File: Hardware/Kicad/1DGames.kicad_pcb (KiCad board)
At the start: 16 copper layers, 530 x 140 mm, 96 parts, among them J1 5V_to_Rail_and_ESP_32_Proto_b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, J10 Edge Pads Right (GND), J13 Edge_Pads_Right_Top, J14 5V LED Strips Long Side Rail, J15 Edge_Pads_Right_Bottom, J16 GND Long Side Rail, J17 MCP23017_Control, J18 Player1_TM1637, J19 CP TM1637, J2 MAX98357_AMPLIFIER_MODULE_OUT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, J20 Player2_TM1637, J22 MCP23017_Gpios, J23 Edge_Pads_Left_Top, J24 Edge_Pads_Left_Bottom, J26 5V/GND from Power Board, J31 MAX98357_AMPLIFIER_MODULE, J32 LCD1602, J34 INMP441_LEFT, J35 INMP441_RIGHT, J36 Led Strip 1 Begin, J37 Led Strip 2 Begin, J38 Led Strip 3 Begin, J39 Led Strip 4 Begin, J40 Led Strip 5 Begin, J42 Led Strip 1 End, J43 Led Strip 2 End, J44 Led Strip 3 End, J45 Led Strip 4 End, J46 Led Strip 5 End, J5 Micro SD Card Reader, J6 5V_15A_Power, J7 DE9_Socket, J8 DE9_Socket, J9 Edge Pads Left (5V), P1 IEC_60320_C13_Plug, Q1 2N2222, SW1 System_Button, U1 AMS1117-3.3, U3 BOB-12009, U4 DEVKIT_V1_ESP32-WROOM-32, U5 74AHCT125

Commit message: Replaced 1602 to 2004 in Kicad and Tinkercad
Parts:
- R26: value 4.7K -> 10K
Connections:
- net /ESP32 & SPI/I2S_BCLK renamed /Audio (page 4) (pagina 4)/I2S_BCLK
- net /ESP32 & SPI/I2S_INMP441_DIN renamed /Audio (page 4) (pagina 4)/I2S_INMP441_DIN
- net /ESP32 & SPI/I2S_MAX98357 renamed /Audio (page 4) (pagina 4)/I2S_MAX98357
- net /ESP32 & SPI/I2S_WS_LRCLK renamed /Audio (page 4) (pagina 4)/I2S_WS_LRCLK
- net /ESP32 & SPI/PASSIVE_BUZZER_SIGNAL renamed /Audio (page 4) (pagina 4)/PASSIVE_BUZZER_SIGNAL
- net /Edge Pads/5V_BUZZER_EXT renamed /Audio (page 4) (pagina 4)/5V_BUZZER_EXT
- net /Edge Pads/I2S_BCLK_OUT renamed /Audio (page 4) (pagina 4)/I2S_BCLK_OUT
- net /Edge Pads/I2S_WS_LRCLK_OUT renamed /Audio (page 4) (pagina 4)/I2S_WS_LRCLK_OUT
- C14 pad 1: /ESP32 & SPI/3V3 -> /Audio (page 4) (pagina 4)/3V3
- C19 pad 1: /I2C/SYSTEM_BUTTON -> /Audio (page 4) (pagina 4)/3V3
- C4 pad 2: /ESP32 & SPI/3V3 -> /Audio (page 4) (pagina 4)/3V3
- C5 pad 2: /ESP32 & SPI/3V3 -> /Audio (page 4) (pagina 4)/3V3
- J17 pad 1: /ESP32 & SPI/3V3 -> /Audio (page 4) (pagina 4)/3V3
- J17 pad 7: /ESP32 & SPI/3V3 -> /Audio (page 4) (pagina 4)/3V3
- J22 pad 2: /ESP32 & SPI/3V3 -> /Audio (page 4) (pagina 4)/3V3
- J23 pad 1: /ESP32 & SPI/3V3 -> /Audio (page 4) (pagina 4)/3V3
- J23 pad 10: /ESP32 & SPI/3V3 -> /Audio (page 4) (pagina 4)/3V3
- J23 pad 11: /ESP32 & SPI/3V3 -> /Audio (page 4) (pagina 4)/3V3
- J23 pad 12: /ESP32 & SPI/3V3 -> /Audio (page 4) (pagina 4)/3V3
- J23 pad 13: /ESP32 & SPI/3V3 -> /Audio (page 4) (pagina 4)/3V3
- J23 pad 2: /ESP32 & SPI/3V3 -> /Audio (page 4) (pagina 4)/3V3
- J23 pad 3: /ESP32 & SPI/3V3 -> /Audio (page 4) (pagina 4)/3V3
- J23 pad 4: /ESP32 & SPI/3V3 -> /Audio (page 4) (pagina 4)/3V3
- J23 pad 5: /ESP32 & SPI/3V3 -> /Audio (page 4) (pagina 4)/3V3
- J23 pad 6: /ESP32 & SPI/3V3 -> /Audio (page 4) (pagina 4)/3V3
- J23 pad 7: /ESP32 & SPI/3V3 -> /Audio (page 4) (pagina 4)/3V3
- J23 pad 8: /ESP32 & SPI/3V3 -> /Audio (page 4) (pagina 4)/3V3
- J23 pad 9: /ESP32 & SPI/3V3 -> /Audio (page 4) (pagina 4)/3V3
- J31 pad 5: /ESP32 & SPI/3V3 -> /Audio (page 4) (pagina 4)/3V3
- J34 pad 2: /ESP32 & SPI/3V3 -> /Audio (page 4) (pagina 4)/3V3
- R1 pad 1: /ESP32 & SPI/3V3 -> /Audio (page 4) (pagina 4)/3V3
- R17 pad 1: /ESP32 & SPI/3V3 -> /Audio (page 4) (pagina 4)/3V3
- R18 pad 1: /ESP32 & SPI/3V3 -> /Audio (page 4) (pagina 4)/3V3
- R19 pad 1: /ESP32 & SPI/3V3 -> /Audio (page 4) (pagina 4)/3V3
- R2 pad 2: /ESP32 & SPI/3V3 -> /Audio (page 4) (pagina 4)/3V3
- R20 pad 1: /ESP32 & SPI/3V3 -> /Audio (page 4) (pagina 4)/3V3
- R21 pad 1: /ESP32 & SPI/3V3 -> /Audio (page 4) (pagina 4)/3V3
- R22 pad 1: /ESP32 & SPI/3V3 -> /Audio (page 4) (pagina 4)/3V3
- R23 pad 1: /ESP32 & SPI/3V3 -> /Audio (page 4) (pagina 4)/3V3
- R24 pad 1: /ESP32 & SPI/3V3 -> /Audio (page 4) (pagina 4)/3V3
- R25 pad 1: /ESP32 & SPI/3V3 -> /Audio (page 4) (pagina 4)/3V3
- R26 pad 1: /ESP32 & SPI/3V3 -> /Audio (page 4) (pagina 4)/3V3
- R28 pad 1: /ESP32 & SPI/3V3 -> /Audio (page 4) (pagina 4)/3V3
- U1 pad 2: /ESP32 & SPI/3V3 -> /Audio (page 4) (pagina 4)/3V3
- U3 pad LV: /ESP32 & SPI/3V3 -> /Audio (page 4) (pagina 4)/3V3
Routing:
- net /ESP32 & SPI/3V3: track 1167.3 -> 0.00 mm, vias 9 -> 0
- net /Audio (page 4) (pagina 4)/3V3: track 0.00 -> 1167.3 mm, vias 0 -> 9

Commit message: New architecture, L1 composition finished, probably, on ESP32
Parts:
- added R29: 10K, Resistor_THT:R_Axial_DIN0204_L3.6mm_D1.6mm_P5.08mm_Horizontal, F.Cu at (326.7, 358.6)
- J32: value LCD1602 -> LCD2004
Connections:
- J22 pad 3: unconnected-(J22-Pin_3-Pad3) -> /ESP32 & SPI/MCP23017_INT_AB
- U4 pad 13: unconnected-(U4-IO12-Pad13) -> /ESP32 & SPI/MCP23017_INT_AB
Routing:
- net /Audio (page 4) (pagina 4)/3V3: track 1167.3 -> 1586.5 mm, vias 9 -> 11
- net /ESP32 & SPI/MCP23017_INT_AB: track 0.00 -> 49.7 mm
- net /I2C/SYSTEM_BUTTON: track 218.5 -> 208.6 mm

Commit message: Broken code, halfway joystick gdi
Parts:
- added C20: 100 nF, Capacitor_THT:CP_Radial_D5.0mm_P2.50mm, F.Cu at (442.6, 415.8)
- added C21: 100 nF, Capacitor_THT:CP_Radial_D5.0mm_P2.50mm, F.Cu at (442.6, 422.3)
- added C22: 100 nF, Capacitor_THT:CP_Radial_D5.0mm_P2.50mm, F.Cu at (442.6, 428.9)
- added C23: 100 nF, Capacitor_THT:CP_Radial_D5.0mm_P2.50mm, F.Cu at (442.6, 435.4)
- added U10: HC-SR04_Ultrasonic_Sensor, PCM_SL_Breakout_Boards:HC-SR04_Ultrasonic_Sensor, F.Cu at (686.2, 332.9)
- added U11: HC-SR04_Ultrasonic_Sensor, PCM_SL_Breakout_Boards:HC-SR04_Ultrasonic_Sensor, F.Cu at (163.2, 273.0)
- added U7: BOB-12009, BOB-12009:CONV_BOB-12009, F.Cu at (284.7, 355.8)
- added U8: HC-SR04_Ultrasonic_Sensor, PCM_SL_Breakout_Boards:HC-SR04_Ultrasonic_Sensor, F.Cu at (159.2, 381.5)
- added U9: HC-SR04_Ultrasonic_Sensor, PCM_SL_Breakout_Boards:HC-SR04_Ultrasonic_Sensor, F.Cu at (685.2, 284.2)
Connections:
- J23 pad 16: unconnected-(J23-Pin_16-Pad16) -> /Edge Pads/HC_SR04_ECHO_1
- J23 pad 17: unconnected-(J23-Pin_17-Pad17) -> /Edge Pads/HC_SR04_TRIG_1
- J23 pad 18: unconnected-(J23-Pin_18-Pad18) -> /Edge Pads/HC_SR04_ECHO_2
- J23 pad 19: unconnected-(J23-Pin_19-Pad19) -> /Edge Pads/HC_SR04_TRIG_2
- J23 pad 20: unconnected-(J23-Pin_20-Pad20) -> /Edge Pads/HC_SR04_ECHO_3
- J23 pad 21: unconnected-(J23-Pin_21-Pad21) -> /Edge Pads/HC_SR04_TRIG_3
- J23 pad 22: unconnected-(J23-Pin_22-Pad22) -> /Edge Pads/HC_SR04_ECHO_4
- J23 pad 23: unconnected-(J23-Pin_23-Pad23) -> /Edge Pads/HC_SR04_TRIG_4
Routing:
- net /Audio (page 4) (pagina 4)/3V3: track 1586.5 -> 1625.2 mm
- net GND: track 7278.8 -> 7306.2 mm
- net /ESP32 & SPI/5V_BOARD: track 1469.0 -> 1487.2 mm
- net /Audio (page 4) (pagina 4)/PASSIVE_BUZZER_SIGNAL: track 85.9 -> 91.3 mm

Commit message: Added Kicad proto board
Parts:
- removed BZ1: Buzzer_5V, Buzzer_Beeper:MagneticBuzzer_ProSignal_ABT-410-RC
- removed C1, C10, C13, C7, C8: 0.1uF, Capacitor_THT:C_Disc_D3.0mm_W1.6mm_P2.50mm
- removed C12: 10-47uF, Capacitor_THT:CP_Radial_D5.0mm_P2.50mm
- removed C14: 1-10uF, Capacitor_THT:CP_Radial_D5.0mm_P2.50mm
- removed C15: 1000 uF, Capacitor_THT:CP_Radial_D10.0mm_P2.50mm
- removed C18: 100uF, Capacitor_THT:CP_Radial_D5.0mm_P2.50mm
- removed C19: 100nF, Capacitor_THT:CP_Radial_D5.0mm_P2.50mm
- removed C20, C21, C22, C23: 100 nF, Capacitor_THT:CP_Radial_D5.0mm_P2.50mm
- removed D2: Player 1 LED, LED_THT:LED_D5.0mm
- removed D3: Player 2 LED, LED_THT:LED_D5.0mm
- removed D4, D5, D6: LED, LED_THT:LED_D5.0mm
- removed J13: Edge_Pads_Right_Top, Connector_PinHeader_2.54mm:PinHeader_1x27_P2.54mm_Vertical_SMD_Pin1Left
- removed J14: 5V LED Strips Long Side Rail, Connector_PinHeader_2.54mm:PinHeader_1x10_P2.54mm_Vertical_SMD_Pin1Left
- removed J15: Edge_Pads_Right_Bottom, Connector_PinHeader_2.54mm:PinHeader_1x27_P2.54mm_Vertical_SMD_Pin1Left
- removed J16: GND Long Side Rail, Connector_PinHeader_2.54mm:PinHeader_1x16_P2.54mm_Vertical_SMD_Pin1Left
- removed J18: Player1_TM1637, PCM_SparkFun-Connector:ScrewTerminal_1x04_P3.5mm_Locking
- removed J19: CP TM1637, PCM_SparkFun-Connector:ScrewTerminal_1x04_P3.5mm_Locking
- removed J2: MAX98357_AMPLIFIER_MODULE_OUTPUT, PCM_SparkFun-Connector:ScrewTerminal_1x02_P5.0mm
- removed J20: Player2_TM1637, PCM_SparkFun-Connector:ScrewTerminal_1x04_P3.5mm_Locking
- removed J23: Edge_Pads_Left_Top, Connector_PinHeader_2.54mm:PinHeader_1x27_P2.54mm_Vertical_SMD_Pin1Left
- removed J24: Edge_Pads_Left_Bottom, Connector_PinHeader_2.54mm:PinHeader_1x27_P2.54mm_Vertical_SMD_Pin1Left
- removed J32: LCD2004, PCM_SparkFun-Connector:ScrewTerminal_1x04_P3.5mm_Horizontal
- removed J34: INMP441_LEFT, TerminalBlock_TE-Connectivity:TerminalBlock_TE_282834-3_1x03_P2.54mm_Horizontal
- removed J35: INMP441_RIGHT, TerminalBlock_TE-Connectivity:TerminalBlock_TE_282834-3_1x03_P2.54mm_Horizontal
- removed J36: Led Strip 1 Begin, PCM_SparkFun-Connector:ScrewTerminal_1x03_P5.0mm
- removed J37: Led Strip 2 Begin, PCM_SparkFun-Connector:ScrewTerminal_1x03_P5.0mm
- removed J38: Led Strip 3 Begin, PCM_SparkFun-Connector:ScrewTerminal_1x03_P5.0mm
- removed J39: Led Strip 4 Begin, PCM_SparkFun-Connector:ScrewTerminal_1x03_P5.0mm
- removed J40: Led Strip 5 Begin, PCM_SparkFun-Connector:ScrewTerminal_1x03_P5.0mm
- removed J42: Led Strip 1 End, PCM_SparkFun-Connector:ScrewTerminal_1x03_P5.0mm
- removed J43: Led Strip 2 End, PCM_SparkFun-Connector:ScrewTerminal_1x03_P5.0mm
- removed J44: Led Strip 3 End, PCM_SparkFun-Connector:ScrewTerminal_1x03_P5.0mm
- removed J45: Led Strip 4 End, PCM_SparkFun-Connector:ScrewTerminal_1x03_P5.0mm
- removed J46: Led Strip 5 End, PCM_SparkFun-Connector:ScrewTerminal_1x03_P5.0mm
- removed J7, J8: DE9_Socket, PCM_SparkFun-Connector:DE9_Header_Horizontal_PTH
- removed LS1: Speaker, Buzzer_Beeper:Speaker_CUI_CMR-1206S-67
- removed P1: IEC_60320_C13_Plug, Connector_PinHeader_2.54mm:PinHeader_1x03_P2.54mm_Vertical
- removed R10, R11, R13, R14, R15, R16: 100-200R, Resistor_THT:R_Axial_DIN0204_L3.6mm_D1.6mm_P5.08mm_Horizontal
- removed R12, R9: 100R, Resistor_THT:R_Axial_DIN0204_L3.6mm_D1.6mm_P5.08mm_Horizontal
- removed R29: 10K, Resistor_THT:R_Axial_DIN0204_L3.6mm_D1.6mm_P5.08mm_Horizontal
- removed SW1: System_Button, Button_Switch_THT:SW_CW_GPTS203211B
- removed U10, U11, U8, U9: HC-SR04_Ultrasonic_Sensor, PCM_SL_Breakout_Boards:HC-SR04_Ultrasonic_Sensor
- removed U4: DEVKIT_V1_ESP32-WROOM-32, PCM_Espressif:ESP32-DevKitC
- added H1: MountingHole_M3, MountingHole:MountingHole_3.2mm_M3, F.Cu at (398.0, 272.8)
- added H2: MountingHole_M3, MountingHole:MountingHole_3.2mm_M3, F.Cu at (378.4, 363.9)
- added H3: MountingHole_M3, MountingHole:MountingHole_3.2mm_M3, F.Cu at (305.4, 335.6)
- added H4: MountingHole_M3, MountingHole:MountingHole_3.2mm_M3, F.Cu at (307.6, 283.6)
- added J11: Conn_01x03, Connector_JST:JST_XH_B3B-XH-A_1x03_P2.50mm_Vertical, F.Cu at (383.0, 274.6)
- added J25: Conn_01x06, Connector_JST:JST_XH_B6B-XH-A_1x06_P2.50mm_Vertical, F.Cu at (397.5, 363.8)
- added J27: Conn_01x06, Connector_JST:JST_XH_B6B-XH-A_1x06_P2.50mm_Vertical, F.Cu at (363.5, 274.6)
- added J3: Conn_01x05, Connector_JST:JST_XH_B5B-XH-A_1x05_P2.50mm_Vertical, F.Cu at (346.5, 274.6)
- added J4: Conn_01x05, Connector_JST:JST_XH_B5B-XH-A_1x05_P2.50mm_Vertical, F.Cu at (329.5, 274.6)
- added R30: 150, PCM_Resistor_SMD_AKL:R_0805_2012Metric_Pad1.20x1.40mm_HandSolder, F.Cu at (381.2, 357.8)
- added R31: 150, PCM_Resistor_SMD_AKL:R_0805_2012Metric_Pad1.20x1.40mm_HandSolder, F.Cu at (383.8, 357.8)
- added R32: 150R, PCM_Resistor_SMD_AKL:R_0805_2012Metric_Pad1.20x1.40mm_HandSolder, F.Cu at (388.8, 348.3)
- added R33: 150R, PCM_Resistor_SMD_AKL:R_0805_2012Metric_Pad1.20x1.40mm_HandSolder, F.Cu at (388.8, 350.8)
- added R34: 150R, PCM_Resistor_SMD_AKL:R_0805_2012Metric_Pad1.20x1.40mm_HandSolder, F.Cu at (388.8, 345.8)
- added R35: 100, PCM_Resistor_SMD_AKL:R_0805_2012Metric_Pad1.20x1.40mm_HandSolder, F.Cu at (391.2, 357.8)
- added R36: 100, PCM_Resistor_SMD_AKL:R_0805_2012Metric_Pad1.20x1.40mm_HandSolder, F.Cu at (388.8, 357.8)
- added R37: 150R, PCM_Resistor_SMD_AKL:R_0805_2012Metric_Pad1.20x1.40mm_HandSolder, F.Cu at (388.8, 343.3)
- added REF**: KiCad-Logo2_6mm_SilkScreen, Symbol:KiCad-Logo2_6mm_SilkScreen, F.Cu at (331.0, 311.9)
- added U12: ESP32-S3-DEVKIT-C1, PCM_Espressif:ESP32-S3-DevKitC, F.Cu at (309.4, 366.4)
- C11, C16, C17, C2, C4: footprint Capacitor_THT:C_Disc_D3.0mm_W1.6mm_P2.50mm -> Capacitor_SMD:C_0805_2012Metric_Pad1.18x1.45mm_HandSolder
- C3, C5: value 10-22uF -> 22uF
- D1: footprint PCM_Diode_THT_AKL:D_DO-41_SOD81_P7.62mm_Horizontal -> Diode_SMD:D_SOD-123
- J1: value 5V_to_Rail_and_ESP_32_Proto_board -> Conn_01x06; footprint PCM_SparkFun-Connector:ScrewTerminal_1x03_P5.0mm -> Connector_JST:JST_XH_B6B-XH-A_1x06_P2.50mm_Vertical
- J10: value Edge Pads Right (GND) -> LED Strips Output; footprint Connector_PinSocket_2.54mm:PinSocket_1x04_P2.54mm_Vertical_SMD_Pin1Left -> TerminalBlock_Phoenix:TerminalBlock_Phoenix_MKDS-1,5-4_1x04_P5.00mm_Horizontal
- J26: value 5V/GND from Power Board -> 5V/GND Rail; footprint PCM_SparkFun-Connector:ScrewTerminal_1x02_P5.0mm -> TerminalBlock_Phoenix:TerminalBlock_Phoenix_MKDS-1,5-2_1x02_P5.00mm_Horizontal
- J6: value 5V_15A_Power -> Conn_01x06; footprint Connector_PinSocket_2.54mm:PinSocket_1x07_P2.54mm_Vertical -> Connector_JST:JST_XH_B6B-XH-A_1x06_P2.50mm_Vertical
- J9: value Edge Pads Left (5V) -> Power In; footprint Connector_PinSocket_2.54mm:PinSocket_1x04_P2.54mm_Vertical_SMD_Pin1Left -> TerminalBlock_Phoenix:TerminalBlock_Phoenix_MKDS-1,5-4_1x04_P5.00mm_Horizontal
- R1, R17, R18, R19, R2, R20, R21, R22, R23, R24, R25, R26, R28, R8: footprint Resistor_THT:R_Axial_DIN0204_L3.6mm_D1.6mm_P5.08mm_Horizontal -> PCM_Resistor_SMD_AKL:R_0805_2012Metric_Pad1.20x1.40mm_HandSolder
- R27: value 10K -> 2.2K; footprint Resistor_THT:R_Axial_DIN0204_L3.6mm_D1.6mm_P5.08mm_Horizontal -> PCM_Resistor_SMD_AKL:R_0805_2012Metric_Pad1.20x1.40mm_HandSolder
- R3, R4, R5, R6, R7: value 220-270 -> 270; footprint Resistor_THT:R_Axial_DIN0204_L3.6mm_D1.6mm_P5.08mm_Horizontal -> PCM_Resistor_SMD_AKL:R_0805_2012Metric_Pad1.20x1.40mm_HandSolder
- moved C11 272.3 mm to (373.0, 283.8), turned to 0 degrees
- moved C6 269.0 mm to (371.9, 290.8), turned to 0 degrees
- moved D1 267.3 mm to (373.4, 312.6), turned to 180 degrees
- moved J6 257.6 mm to (310.0, 274.6), turned to 0 degrees
- moved J10 248.9 mm to (393.2, 319.8), turned to 90 degrees
- moved J9 239.9 mm to (393.2, 298.3), turned to 90 degrees
- moved J1 233.0 mm to (395.5, 338.3)
- moved C9 212.3 mm to (372.0, 303.1), turned to 0 degrees
- moved J26 167.4 mm to (393.2, 331.3), turned to 90 degrees
- moved U1 149.6 mm to (379.6, 328.3), turned to 0 degrees
- moved C3 140.4 mm to (381.2, 322.1), turned to 90 degrees
- moved C2 138.8 mm to (377.0, 319.5), turned to 90 degrees
- moved C5 137.5 mm to (380.8, 337.3), turned to 90 degrees
- moved C4 134.9 mm to (376.0, 335.8), turned to 90 degrees
- moved Q1 125.0 mm to (374.2, 349.8)
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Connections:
- C11 pad 2: /Led Strips/5V -> Net-(D1-A)
- C16 pad 1: /ESP32 & SPI/5V_BOARD -> /ESP32 & SPI/5V
- C17 pad 1: /ESP32 & SPI/5V_BOARD -> /ESP32 & SPI/5V
- C2 pad 2: /ESP32 & SPI/5V_BOARD -> /ESP32 & SPI/5V
- C3 pad 2: /ESP32 & SPI/5V_BOARD -> /ESP32 & SPI/5V
- C6 pad 2: /Led Strips/5V -> Net-(D1-A)
- C9 pad 2: /Led Strips/5V -> Net-(D1-A)
- D1 pad 1: /ESP32 & SPI/5V_BOARD -> /ESP32 & SPI/5V
- D1 pad 2: /Led Strips/5V -> Net-(D1-A)
- J1 pad 1: /ESP32 & SPI/5V_BOARD -> /JST Connectors/TM1637_SHARED_CLK_OUT
- J1 pad 2: /ESP32 & SPI/5V_BOARD -> /JST Connectors/TM1637_SHARED_CLK_OUT
- J1 pad 3: GND -> /JST Connectors/TM1637_SHARED_CLK_OUT
- J10 pad 1: GND -> Net-(D1-A)
- J10 pad 2: GND -> Net-(D1-A)
- J26 pad 1: /ESP32 & SPI/5V_BOARD -> /ESP32 & SPI/5V
- J31 pad 7: /ESP32 & SPI/5V_BOARD -> /ESP32 & SPI/5V
- J5 pad 5: /ESP32 & SPI/5V_BOARD -> /ESP32 & SPI/5V
- J6 pad 1: Net-(J6-Pin_1) -> /I2C/P1_LED_OUT
- J6 pad 2: Net-(J6-Pin_2) -> /I2C/P2_LED_OUT
- J6 pad 3: Net-(J6-Pin_3) -> /I2C/SELECT_LED_OUT
- J6 pad 4: /Led Strips/5V -> /I2C/PLAY_PAUSE_LED_OUT
- J6 pad 5: GND -> /I2C/SETTINGS_LED_OUT
- J6 pad 6: /Led Strips/5V -> /I2C/SYSTEM_BUTTON
- J9 pad 1: /Led Strips/5V -> Net-(D1-A)
- J9 pad 2: /Led Strips/5V -> Net-(D1-A)
- J9 pad 3: /Led Strips/5V -> GND
- J9 pad 4: /Led Strips/5V -> GND
- R3 pad 1: /Edge Pads/P2_LED_OUT -> /I2C/P2_LED_OUT
- R4 pad 1: /Edge Pads/P1_LED_OUT -> /I2C/P1_LED_OUT
- R5 pad 1: /Edge Pads/PLAY_PAUSE_LED_OUT -> /I2C/PLAY_PAUSE_LED_OUT
- R6 pad 2: /Edge Pads/SELECT_LED_OUT -> /I2C/SELECT_LED_OUT
- R7 pad 2: /Edge Pads/SETTINGS_LED_OUT -> /I2C/SETTINGS_LED_OUT
- R8 pad 1: /Edge Pads/LED_STRIP_DATA_5V -> /JST Connectors/LED_STRIP_DATA_5V
- U1 pad 3: /ESP32 & SPI/5V_BOARD -> /ESP32 & SPI/5V
- U3 pad HV: /ESP32 & SPI/5V_BOARD -> /ESP32 & SPI/5V
- U3 pad HV2: /Edge Pads/I2C_SCL_5V -> /I2C/I2C_SCL_5V
- U3 pad HV3: /Edge Pads/I2C_SDA_5V -> /I2C/I2C_SDA_5V
- U5 pad 10: /ESP32 & SPI/5V_BOARD -> /ESP32 & SPI/5V
- U5 pad 13: /ESP32 & SPI/5V_BOARD -> /ESP32 & SPI/5V
- U5 pad 14: /ESP32 & SPI/5V_BOARD -> /ESP32 & SPI/5V
- U5 pad 4: /ESP32 & SPI/5V_BOARD -> /ESP32 & SPI/5V
- U7 pad HV: /ESP32 & SPI/5V_BOARD -> /ESP32 & SPI/5V
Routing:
- net GND: track 7306.2 -> 2.47 mm, vias 18 -> 65
- net /ESP32 & SPI/5V_BOARD: track 1487.2 -> 0.00 mm, vias 11 -> 0
- net /Audio (page 4) (pagina 4)/3V3: track 1625.2 -> 318.9 mm, vias 11 -> 7
- net /Led Strips/5V: track 1185.9 -> 0.00 mm
- net /Edge Pads/TM1637_SHARED_CLK_OUT: track 732.1 -> 0.00 mm, vias 5 -> 0
- net /I2C/P2_JOYSTICK_LEFT: track 475.6 -> 63.6 mm, vias 1 -> 3
- net /Edge Pads/P2_LED_OUT: track 405.4 -> 0.00 mm, vias 4 -> 0
- net /I2C/P2_JOYSTICK_RIGHT: track 460.4 -> 60.6 mm, vias 2 -> 3
- net /I2C/P2_JOYSTICK_UP: track 448.0 -> 58.3 mm, vias 2 -> 3
- net /I2C/P2_JOYSTICK_BUTTON: track 443.8 -> 54.2 mm, vias 2 -> 3
- net /I2C/P2_JOYSTICK_DOWN: track 442.5 -> 56.6 mm
- net /Edge Pads/P2_TM1637_DIN_OUT: track 329.7 -> 0.00 mm, vias 2 -> 0
- net /ESP32 & SPI/5V: track 0.00 -> 294.0 mm, vias 0 -> 3
- net /I2C/P1_JOYSTICK_BUTTON: track 342.1 -> 48.2 mm, vias 2 -> 0
- net /I2C/P1_JOYSTICK_DOWN: track 325.2 -> 58.2 mm, vias 3 -> 0
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- added copper zone on B.Cu, net GND
- added copper zone on F.Cu, net GND
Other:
- board size 530 x 140 mm -> 100 x 100 mm
- board text added: "-"
- board text added: "1E"
- board text added: "1T"
- board text added: "2E"
- board text added: "2T"
- board text added: "3E"
- board text added: "3T"
- board text added: "4E"
- board text added: "4T"
- board text added: "5V"
- board text added: "74AHCT125"
- board text added: "BK"
- board text added: "BN"
- board text added: "BZ"
- board text added: "CLOCK"
- board text added: "CP"
- board text added: "CS"
- board text added: "D.S.+LED STR."
- board text added: "DIST SENSORS"
- board text added: "DN"
- board text added: "FRAXIS 1.0 (c) 2026 Five Row Arcade Experience Interactive System Designed by Michel Keijzers"
- board text added: "G"
- board text added: "GND"
- board text added: "I2S I2C"
- board text added: "I2S MAX53987"
- board text added: "IN"
- board text added: "L.S."
- board text added: "LED STRIPS POWER"
- board text added: "LEDS/BUTTON"
- board text added: "LT"
- board text added: "LVL SHFTR"
- board text added: "MAIN POWER"
- board text added: "MCP23017"
- board text added: "MI"
- board text added: "MO"
- board text added: "P1"
- board text added: "P1 JOYSTICK"
- board text added: "P2"
- board text added: "P2 JOYSTICK"
- board text added: "PL"
- board text added: "RAIL P."
- board text added: "RT"
- board text added: "SA"
- board text added: "SK"
- board text added: "SL"
- board text added: "SPI SD CARD"
- board text added: "ST"
- board text added: "SU"
- board text added: "TM 1637"
- board text added: "UP"
- board text added: "WS"

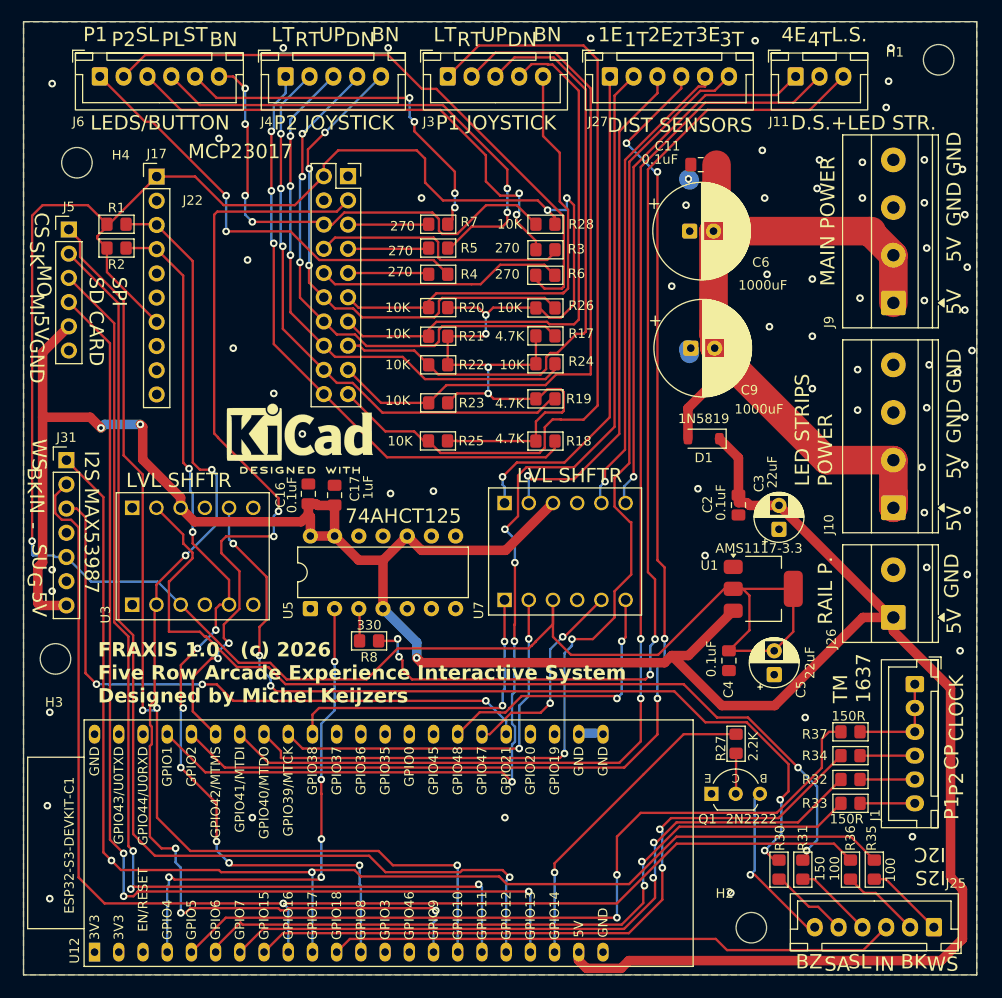
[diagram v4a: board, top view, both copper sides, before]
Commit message: New Fraxis PCB layout
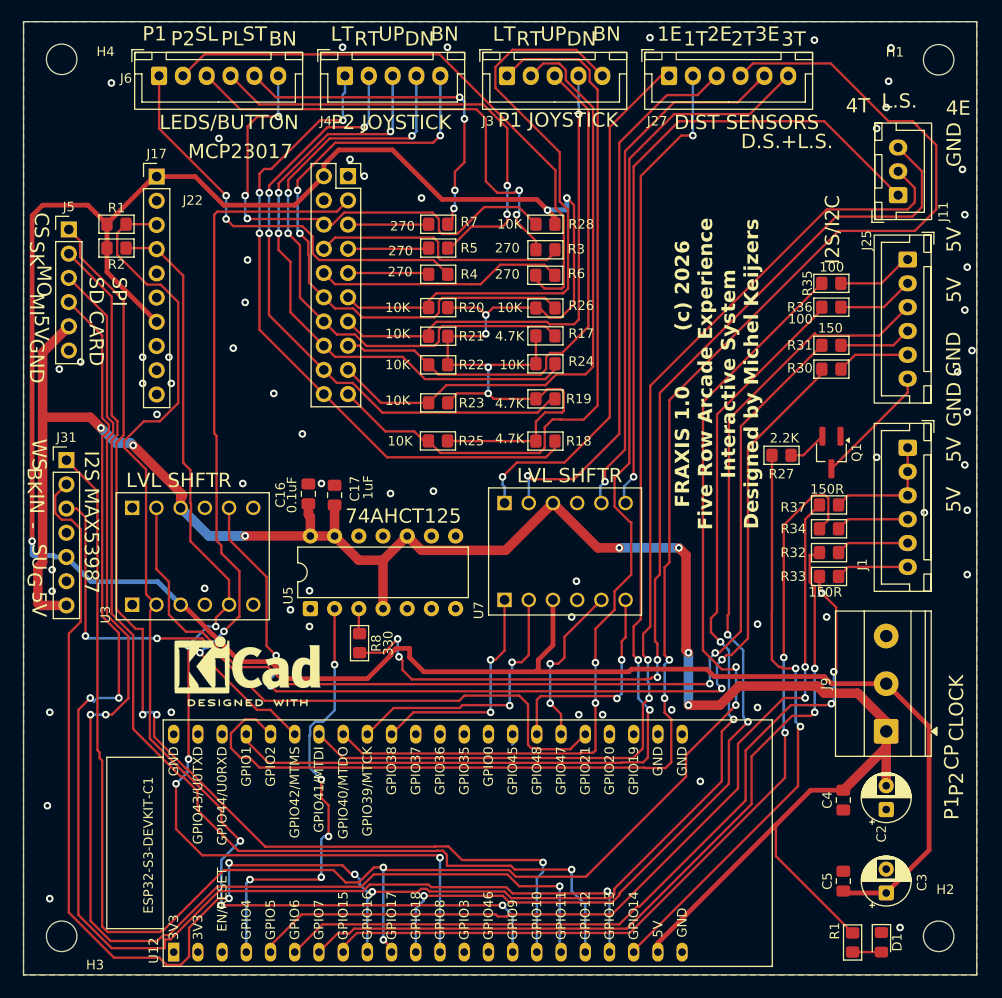
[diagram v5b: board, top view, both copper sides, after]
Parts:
- removed C11: 0.1uF, Capacitor_SMD:C_0805_2012Metric_Pad1.18x1.45mm_HandSolder
- removed C6, C9: 1000uF, Capacitor_THT:CP_Radial_D10.0mm_P2.50mm
- removed J10: LED Strips Output, TerminalBlock_Phoenix:TerminalBlock_Phoenix_MKDS-1,5-4_1x04_P5.00mm_Horizontal
- removed J26: 5V/GND Rail, TerminalBlock_Phoenix:TerminalBlock_Phoenix_MKDS-1,5-2_1x02_P5.00mm_Horizontal
- removed U1: AMS1117-3.3, Package_TO_SOT_SMD:SOT-223-3_TabPin2
- added R1: R, PCM_Resistor_SMD_AKL:R_0805_2012Metric_Pad1.20x1.40mm_HandSolder, F.Cu at (389.0, 365.4)
- C2: value 0.1uF -> 22 uF; footprint Capacitor_SMD:C_0805_2012Metric_Pad1.18x1.45mm_HandSolder -> Capacitor_THT:CP_Radial_D5.0mm_P2.50mm
- C3: value 22uF -> 10 uF
- C4: value 0.1uF -> 0.1 uF
- C5: value 22uF -> 0.1 uF; footprint Capacitor_THT:CP_Radial_D5.0mm_P2.50mm -> Capacitor_SMD:C_0805_2012Metric_Pad1.18x1.45mm_HandSolder
- D1: value 1N5819 -> LED; footprint Diode_SMD:D_SOD-123 -> LED_SMD:LED_0805_2012Metric_Pad1.15x1.40mm_HandSolder
- J9: value Power In -> Conn_01x03; footprint TerminalBlock_Phoenix:TerminalBlock_Phoenix_MKDS-1,5-4_1x04_P5.00mm_Horizontal -> TerminalBlock_Phoenix:TerminalBlock_Phoenix_MKDS-1,5-3_1x03_P5.00mm_Horizontal
- Q1: footprint PCM_Package_TO_SOT_THT_AKL:TO-92L_Inline_Wide_ECB -> Package_TO_SOT_SMD:TSOT-23_HandSoldering
- moved J25 70.1 mm to (394.8, 293.8), turned to -90 degrees
- moved R35 61.7 mm to (386.7, 296.2), turned to 0 degrees
- moved R36 59.0 mm to (386.7, 298.8), turned to 0 degrees
- moved D1 56.0 mm to (392.0, 365.4), turned to -90 degrees
- moved R31 55.1 mm to (386.8, 302.8), turned to 0 degrees
- moved R30 52.8 mm to (386.8, 305.2), turned to 0 degrees
- moved J9 45.0 mm to (392.5, 343.2)
- moved C3 39.8 mm to (392.5, 360.2)
- moved Q1 37.9 mm to (386.8, 314.0), turned to -90 degrees
- moved C2 35.5 mm to (392.5, 351.5)
- moved R27 30.6 mm to (381.5, 314.3), turned to 0 degrees
- moved H3 29.1 mm to (306.0, 364.8)
- moved REF** 25.0 mm to (325.5, 336.2)
- moved J1 24.8 mm to (394.8, 313.5)
- moved R32 23.9 mm to (386.5, 324.5)
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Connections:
- C3 pad 1: GND -> /Audio (page 4) (pagina 4)/3V3
- C3 pad 2: /ESP32 & SPI/5V -> GND
- C4 pad 2: /Audio (page 4) (pagina 4)/3V3 -> /ESP32 & SPI/5V
- C5 pad 1: GND -> /Audio (page 4) (pagina 4)/3V3
- C5 pad 2: /Audio (page 4) (pagina 4)/3V3 -> GND
- D1 pad 1: /ESP32 & SPI/5V -> GND
- D1 pad 2: Net-(D1-A) -> Net-(R1--)
- J9 pad 1: Net-(D1-A) -> /ESP32 & SPI/5V
- J9 pad 2: Net-(D1-A) -> /Audio (page 4) (pagina 4)/3V3
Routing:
- net Net-(D1-A): track 87.1 -> 0.00 mm
- net /ESP32 & SPI/5V: track 294.0 -> 221.5 mm, vias 3 -> 7
- net /Audio (page 4) (pagina 4)/I2S_BCLK: track 134.0 -> 196.9 mm, vias 1 -> 6
- net /Audio (page 4) (pagina 4)/I2S_WS_LRCLK: track 136.9 -> 191.6 mm, vias 2 -> 4
- net /Audio (page 4) (pagina 4)/I2S_INMP441_DIN: track 59.7 -> 108.4 mm, vias 0 -> 3
- net /ESP32 & SPI/HC_SR04_TRIG_2: track 125.3 -> 160.8 mm, vias 4 -> 2
- net /Audio (page 4) (pagina 4)/PASSIVE_BUZZER_SIGNAL: track 34.0 -> 61.6 mm, vias 1 -> 2
- net /ESP32 & SPI/SPI_MISO: track 113.9 -> 138.2 mm
- net /ESP32 & SPI/SPI_MOSI: track 111.0 -> 134.0 mm
- net /ESP32 & SPI/CP_TM1637_DIN: track 73.8 -> 90.5 mm
- net /Audio (page 4) (pagina 4)/3V3: track 318.9 -> 335.5 mm
- net /I2C/I2C_SDA_5V: track 91.0 -> 107.2 mm, vias 5 -> 4
- net /I2C/P1_JOYSTICK_BUTTON: track 48.2 -> 64.4 mm
- net /I2C/I2C_SCL_5V: track 98.7 -> 112.2 mm
- net /ESP32 & SPI/HC_SR04_TRIG_4: track 127.2 -> 114.0 mm
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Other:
- board text added: "D.S.+L.S."
- board text added: "I2S/I2C"
- board text removed: "BZ"
- board text removed: "D.S.+LED STR."
- board text removed: "I2S I2C"
- board text removed: "LED STRIPS POWER"
- board text removed: "MAIN POWER"
- board text removed: "RAIL P."
- board text removed: "SA"
- board text removed: "TM 1637"

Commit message: During highscores
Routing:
- net /I2C/I2C_SDA_5V: track 107.2 -> 125.4 mm
- net /I2C/I2C_SCL_5V: track 112.2 -> 118.9 mm
- net /JST Connectors/LED_STRIP_DATA_5V: track 108.6 -> 104.5 mm
- net /ESP32 & SPI/SPI_MOSI: track 134.0 -> 137.6 mm
- net /ESP32 & SPI/SPI_CS: track 115.2 -> 118.7 mm
- net /Audio (page 4) (pagina 4)/I2S_BCLK: track 196.9 -> 200.2 mm
- net /ESP32 & SPI/LED_STRIP_DATA_3V3: track 47.2 -> 44.4 mm
- net /ESP32 & SPI/SPI_SCK: track 116.4 -> 118.8 mm
- net /ESP32 & SPI/MCP23017_INT_AB: track 77.1 -> 75.2 mm
- net /Audio (page 4) (pagina 4)/I2S_MAX98357: track 75.8 -> 77.0 mm
- net /ESP32 & SPI/I2C_SDA_3V3: track 109.3 -> 108.2 mm
- net /ESP32 & SPI/I2C_SCL_3V3: track 123.3 -> 124.3 mm
- net /Audio (page 4) (pagina 4)/3V3: track 335.5 -> 334.6 mm
- net /Audio (page 4) (pagina 4)/I2S_INMP441_DIN: track 108.4 -> 107.7 mm
- net /ESP32 & SPI/HC_SR04_ECHO_2: track 28.7 -> 28.1 mm
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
